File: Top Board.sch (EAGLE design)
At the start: 22 parts, among them IC1 UA741CDT

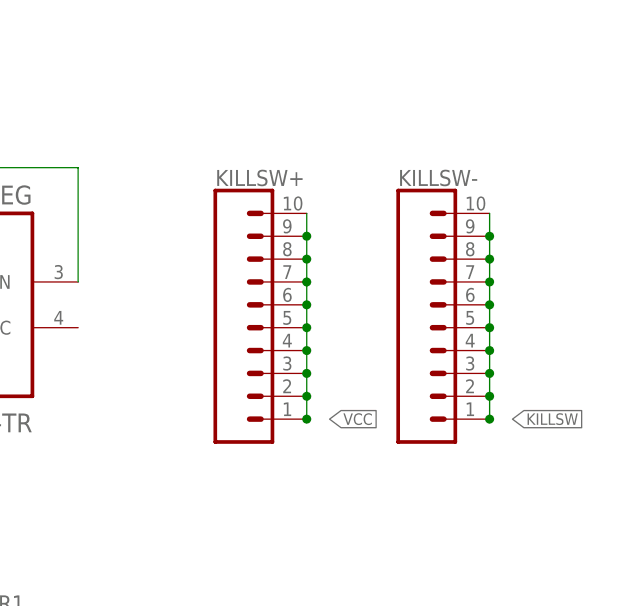
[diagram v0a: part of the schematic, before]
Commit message: Top Board
Rev 1.3 - Hall Effect KILLSW
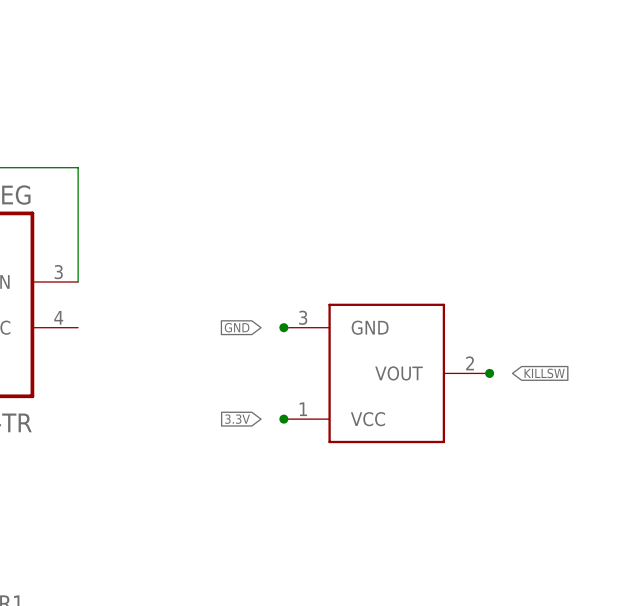
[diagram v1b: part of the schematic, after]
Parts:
- removed KILLSW+, KILLSW-: (no value), SparkFun-Connectors:CONN_10SMD_MALE
- added AH9250: A1324LLHLT-T, Sensor:A1324LLHLT-T
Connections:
- net 3.3V: now also AH9250.VCC
- net GND: now also AH9250.GND
- net KILLSW: now also AH9250.VOUT; no longer KILLSW-.1, KILLSW-.10, KILLSW-.2, KILLSW-.3, KILLSW-.4, KILLSW-.5, KILLSW-.6, KILLSW-.7, KILLSW-.8, KILLSW-.9
- net VCC: no longer KILLSW+.1, KILLSW+.10, KILLSW+.2, KILLSW+.3, KILLSW+.4, KILLSW+.5, KILLSW+.6, KILLSW+.7, KILLSW+.8, KILLSW+.9
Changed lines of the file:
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@@
 <?xml version="1.0" encoding="utf-8"?>
 <!DOCTYPE eagle SYSTEM "eagle.dtd">
-<eagle version="9.5.0">
+<eagle version="9.5.1">
 <drawing>
 <settings>
@@
 <part name="RJ45" library="RJ45 WM14372CT-ND" deviceset="0855437002" device="" value=""/>
 <part name="J1" library="SparkFun-Connectors" library_urn="urn:adsk.eagle:library:513" deviceset="CONN_03" device="SMD_RA_MALE" package3d_urn="urn:adsk.eagle:package:38078/1"/>
-<part name="KILLSW+" library="SparkFun-Connectors" library_urn="urn:adsk.eagle:library:513" deviceset="CONN_10" device="SMD_MALE" package3d_urn="urn:adsk.eagle:package:38163/1"/>
-<part name="KILLSW-" library="SparkFun-Connectors" library_urn="urn:adsk.eagle:library:513" deviceset="CONN_10" device="SMD_MALE" package3d_urn="urn:adsk.eagle:package:38163/1"/>
 <part name="DECODER" library="SN74LVC1G139DCUR" deviceset="SN74LVC1G139DCUR" device=""/>
 <part name="3.3REG" library="MIC5504-3.3YM5-TR" deviceset="MIC5504-3.3YM5-TR" device=""/>
@@
 <part name="C3" library="rcl" library_urn="urn:adsk.eagle:library:334" deviceset="C-US" device="C0805" package3d_urn="urn:adsk.eagle:package:23617/2" value="10uF"/>
 <part name="IC1" library="maxim" library_urn="urn:adsk.eagle:library:269" deviceset="ICL7611" device="SA" package3d_urn="urn:adsk.eagle:package:17511/1" technology="BC" value="UA741CDT"/>
+<part name="AH9250" library="Sensor" library_urn="urn:adsk.eagle:library:11396555" deviceset="A1324LLHLT-T" device="" package3d_urn="urn:adsk.eagle:package:10907352/2"/>
 </parts>
 <sheets>
@@
 <attribute name="NAME" x="22.86" y="43.688" size="1.778" layer="95" font="vector"/>
 </instance>
-<instance part="KILLSW+" gate="G$1" x="40.64" y="129.54" smashed="yes">
-<attribute name="VALUE" x="40.64" y="106.934" size="1.778" layer="96" font="vector"/>
-<attribute name="NAME" x="40.64" y="137.668" size="1.778" layer="95" font="vector"/>
-</instance>
-<instance part="KILLSW-" gate="G$1" x="60.96" y="129.54" smashed="yes">
-<attribute name="VALUE" x="60.96" y="106.934" size="1.778" layer="96" font="vector"/>
-<attribute name="NAME" x="60.96" y="137.668" size="1.778" layer="95" font="vector"/>
-</instance>
 <instance part="DECODER" gate="G$1" x="-2.54" y="58.42" smashed="yes" rot="MR0">
 <attribute name="NAME" x="10.16" y="72.12" size="2.0828" layer="95" ratio="10" rot="SMR0"/>
@@
 <attribute name="VALUE" x="-66.04" y="132.08" size="1.778" layer="96"/>
 </instance>
+<instance part="AH9250" gate="G$1" x="60.96" y="116.84" smashed="yes" rot="R90"/>
 </instances>
 <busses>
@@
 <label x="-104.14" y="144.78" size="1.27" layer="95" rot="R180" xref="yes"/>
 </segment>
+<segment>
+<pinref part="AH9250" gate="G$1" pin="GND"/>
+<junction x="48.26" y="121.92"/>
+<label x="45.72" y="121.92" size="1.016" layer="95" rot="R180" xref="yes"/>
+</segment>
 </net>
 <net name="N$8" class="0">
@@
 </segment>
 <segment>
-<pinref part="KILLSW+" gate="G$1" pin="1"/>
-<pinref part="KILLSW+" gate="G$1" pin="6"/>
-<pinref part="KILLSW+" gate="G$1" pin="7"/>
-<pinref part="KILLSW+" gate="G$1" pin="9"/>
-<pinref part="KILLSW+" gate="G$1" pin="10"/>
-<wire x1="50.8" y1="134.62" x2="50.8" y2="132.08" width="0.1524" layer="91"/>
-<junction x="50.8" y="132.08"/>
-<pinref part="KILLSW+" gate="G$1" pin="8"/>
-<wire x1="50.8" y1="129.54" x2="50.8" y2="132.08" width="0.1524" layer="91"/>
-<junction x="50.8" y="129.54"/>
-<wire x1="50.8" y1="129.54" x2="50.8" y2="127" width="0.1524" layer="91"/>
-<junction x="50.8" y="127"/>
-<wire x1="50.8" y1="127" x2="50.8" y2="124.46" width="0.1524" layer="91"/>
-<junction x="50.8" y="124.46"/>
-<wire x1="50.8" y1="124.46" x2="50.8" y2="121.92" width="0.1524" layer="91"/>
-<pinref part="KILLSW+" gate="G$1" pin="5"/>
-<junction x="50.8" y="121.92"/>
-<wire x1="50.8" y1="121.92" x2="50.8" y2="119.38" width="0.1524" layer="91"/>
-<pinref part="KILLSW+" gate="G$1" pin="4"/>
-<junction x="50.8" y="119.38"/>
-<wire x1="50.8" y1="119.38" x2="50.8" y2="116.84" width="0.1524" layer="91"/>
-<pinref part="KILLSW+" gate="G$1" pin="3"/>
-<junction x="50.8" y="116.84"/>
-<wire x1="50.8" y1="116.84" x2="50.8" y2="114.3" width="0.1524" layer="91"/>
-<pinref part="KILLSW+" gate="G$1" pin="2"/>
-<junction x="50.8" y="114.3"/>
-<wire x1="50.8" y1="114.3" x2="50.8" y2="111.76" width="0.1524" layer="91"/>
-<junction x="50.8" y="111.76"/>
-<label x="53.34" y="111.76" size="1.27" layer="95" xref="yes"/>
-</segment>
-<segment>
 <pinref part="J1" gate="J$1" pin="2"/>
 <junction x="33.02" y="38.1"/>
@@
 </segment>
 <segment>
-<pinref part="KILLSW-" gate="G$1" pin="1"/>
-<wire x1="71.12" y1="111.76" x2="71.12" y2="114.3" width="0.1524" layer="91"/>
-<wire x1="71.12" y1="114.3" x2="71.12" y2="116.84" width="0.1524" layer="91"/>
-<wire x1="71.12" y1="116.84" x2="71.12" y2="119.38" width="0.1524" layer="91"/>
-<wire x1="71.12" y1="119.38" x2="71.12" y2="121.92" width="0.1524" layer="91"/>
-<wire x1="71.12" y1="121.92" x2="71.12" y2="124.46" width="0.1524" layer="91"/>
-<wire x1="71.12" y1="124.46" x2="71.12" y2="127" width="0.1524" layer="91"/>
-<wire x1="71.12" y1="127" x2="71.12" y2="129.54" width="0.1524" layer="91"/>
-<wire x1="71.12" y1="129.54" x2="71.12" y2="132.08" width="0.1524" layer="91"/>
-<wire x1="71.12" y1="132.08" x2="71.12" y2="134.62" width="0.1524" layer="91"/>
-<pinref part="KILLSW-" gate="G$1" pin="2"/>
-<junction x="71.12" y="114.3"/>
-<pinref part="KILLSW-" gate="G$1" pin="3"/>
+<pinref part="AH9250" gate="G$1" pin="VOUT"/>
 <junction x="71.12" y="116.84"/>
-<pinref part="KILLSW-" gate="G$1" pin="4"/>
-<junction x="71.12" y="119.38"/>
-<pinref part="KILLSW-" gate="G$1" pin="5"/>
-<junction x="71.12" y="121.92"/>
-<pinref part="KILLSW-" gate="G$1" pin="6"/>
-<junction x="71.12" y="124.46"/>
-<pinref part="KILLSW-" gate="G$1" pin="7"/>
-<junction x="71.12" y="127"/>
-<pinref part="KILLSW-" gate="G$1" pin="8"/>
-<junction x="71.12" y="129.54"/>
-<pinref part="KILLSW-" gate="G$1" pin="9"/>
-<junction x="71.12" y="132.08"/>
-<pinref part="KILLSW-" gate="G$1" pin="10"/>
-<junction x="71.12" y="111.76"/>
-<label x="73.66" y="111.76" size="1.27" layer="95" xref="yes"/>
+<label x="73.66" y="116.84" size="1.016" layer="95" xref="yes"/>
 </segment>
 </net>
@@
 <label x="-116.84" y="121.92" size="1.27" layer="95" xref="yes"/>
 </segment>
-</net>
+<segment>
+<pinref part="AH9250" gate="G$1" pin="VCC"/>
+<junction x="48.26" y="111.76"/>
+<label x="45.72" y="111.76" size="1.016" layer="95" rot="R180" xref="yes"/>
+</segment>
+</net>
